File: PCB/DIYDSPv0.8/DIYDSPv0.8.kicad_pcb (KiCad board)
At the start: 4 copper layers, 100 x 80 mm, 199 parts, among them J1 Conn_01x06, J2 Conn_01x04, J3 Conn_01x04, J4 Conn_01x05, J5 Conn_01x01, J6 Conn_01x02, U1 ADAU1452, U5 AMS1117-1.2, X1 12.288MHz

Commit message: Updating progress on v0.8 design
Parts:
- removed C1, C14, C19, C24, C25, C27, C3, C31, C32, C34, C51: 10u, Capacitor_SMD:C_0603_1608Metric
- removed C10, C11, C12, C55, C7: 22u, Capacitor_SMD:C_0805_2012Metric
- removed C13, C17, C18, C20, C21, C26, C28, C29, C30, C33, C39, C43, C44, C45, C46, C48, C5, C52, C53, C54, C56, C57, C6: 100n, Capacitor_SMD:C_0402_1005Metric
- removed C15, C16, C2, C4: 2.2u, Capacitor_SMD:C_0402_1005Metric
- removed C22, C23, C40, C41: 10n, Capacitor_SMD:C_0402_1005Metric
- removed C35: 4.7n, Capacitor_SMD:C_0402_1005Metric
- removed C36, C37, C49, C50, C58, C59, C60, C61, C62, C63, C64, C65, C66, C67, C68, C69, C70, C71, C72, C73, C74, C75, C76, C77, C78, C79, C80, C81: 1u, Capacitor_SMD:C_0402_1005Metric
- removed C38: 1n, Capacitor_SMD:C_0402_1005Metric
- removed C42: 100p, Capacitor_SMD:C_0402_1005Metric
- removed C47: 47p, Capacitor_SMD:C_0402_1005Metric
- removed C8, C9: 22p, Capacitor_SMD:C_0402_1005Metric
- removed CN1: ~, Custom:MX126-5.0-02P-GN01-Cu-S-A
- removed D1: ~, Custom:SMF20CA
- removed D2, D3, D4: LED, LED_SMD:LED_0805_2012Metric
- removed J1: Conn_01x06, Connector_PinHeader_2.54mm:PinHeader_1x06_P2.54mm_Vertical
- removed J2, J3: Conn_01x04, Connector_PinHeader_2.54mm:PinHeader_1x04_P2.54mm_Vertical
- removed J4: Conn_01x05, Connector_PinHeader_2.54mm:PinHeader_1x05_P2.54mm_Vertical
- removed J5: Conn_01x01, Connector_PinHeader_2.54mm:PinHeader_1x01_P2.54mm_Vertical
- removed J6: Conn_01x02, Connector_PinHeader_2.54mm:PinHeader_1x02_P2.54mm_Vertical
- removed R1, R10, R11, R17, R18, R19, R2, R23, R24, R3, R4, R5, R6, R7, R8, R9: 100, Resistor_SMD:R_0805_2012Metric
- removed R12, R13, R25, R26, R27, R28: 10k, Resistor_SMD:R_0402_1005Metric
- removed R14, R29, R30, R37, R38, R39, R40, R41, R42, R43, R44, R45, R46, R49, R50, R57, R58, R59, R60, R61, R62, R63, R64, R65, R66: 100k, Resistor_SMD:R_0402_1005Metric
- removed R15, R16: 2.2k, Resistor_SMD:R_0402_1005Metric
- removed R20: 1k, Resistor_SMD:R_0402_1005Metric
- removed R21, R22: 5.1k, Resistor_SMD:R_0402_1005Metric
- removed R31, R32, R33, R34, R35, R36, R47, R48, R51, R52, R53, R54, R55, R56, R67, R68: 220k, Resistor_SMD:R_0603_1608Metric
- removed TP1, TP3, TP4, TP6: TestPoint, TestPoint:TestPoint_THTPad_D4.0mm_Drill2.0mm
- removed TP10, TP11, TP12, TP13, TP14, TP15, TP2, TP5, TP7, TP8, TP9: TestPoint, TestPoint:TestPoint_THTPad_D2.0mm_Drill1.0mm
- removed U1: ADAU1452, Custom:ADAU1452WBCPZ-RL
- removed U10: ~, Custom:GT-USB-7010ASV
- removed U11, U12, U13, U14, U15, U16, U8, U9: ~, Custom:PJ-320D
- removed U17: ~, Custom:ESP32-S3-WROOM-1U-N8
- removed U18, U19, U7: ~, Custom:YTS1C0033BBG01
- removed U2, U3: ~, Custom:AK4619VN
- removed U20, U21, U22, U23: ~, Custom:LM324DT
- removed U4: ~, Custom:K7803M-1000R3
- removed U5: AMS1117-1.2, Custom:AMS1117-1.2
- removed U6: ~, Custom:ADM811TARTZ-REEL7
- removed X1: 12.288MHz, Custom:S47SMD12.288M20PF20R30B3
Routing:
- net +1V2: track 117.7 -> 0.00 mm, vias 4 -> 0
- net GND: track 99.5 -> 0.00 mm, vias 102 -> 0
- net /SCL: track 89.6 -> 0.00 mm, vias 5 -> 0
- net /SDA: track 89.5 -> 0.00 mm, vias 5 -> 0
- net +3V3: track 80.3 -> 0.00 mm, vias 17 -> 0
- net /DAC_OUT8: track 78.8 -> 0.00 mm, vias 2 -> 0
- net /DAC_OUT7: track 72.9 -> 0.00 mm, vias 2 -> 0
- net /DAC_OUT4: track 72.9 -> 0.00 mm, vias 2 -> 0
- net /MCLK: track 72.8 -> 0.00 mm, vias 3 -> 0
- net /DAC_OUT3: track 68.1 -> 0.00 mm, vias 2 -> 0
- net /DAC_OUT6: track 66.1 -> 0.00 mm, vias 2 -> 0
- net /DAC_OUT5: track 65.9 -> 0.00 mm, vias 2 -> 0
- net /DAC_OUT1: track 64.6 -> 0.00 mm, vias 2 -> 0
- net /DAC_OUT2: track 63.0 -> 0.00 mm, vias 2 -> 0
- net /LRCLK_OUT0: track 59.5 -> 0.00 mm, vias 2 -> 0
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- removed copper zone on In2.Cu, net +12V
- removed copper zone on In2.Cu, net +3V3
- removed copper zone on B.Cu, net GND
- removed copper zone on F.Cu, net GND
- removed copper zone on In1.Cu, net GND
- removed copper zone on In2.Cu, net GND
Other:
- board outline removed
- board text removed: "+ -"
- board text removed: "1/2"
- board text removed: "12V"
- board text removed: "12V DC"
- board text removed: "1V2"
- board text removed: "3/4"
- board text removed: "3V3"
- board text removed: "5/6"
- board text removed: "7/8"
- board text removed: "ANALOG INPUT"
- board text removed: "ANALOG OUTPUT"
- board text removed: "AUXADC 0-5"
- board text removed: "BOOT"
- board text removed: "GND-3V3"
- board text removed: "GND-TX-RX"
- board text removed: "MCL-DSP8x8 V0.7"
- board text removed: "MP 0-3,6"
- board text removed: "Michael Larson"
- board text removed: "Optional BOOT Pull-Up"
- board text removed: "RESET"
- board text removed: "SCL SDA"

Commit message: More progress on V0.8 layout. Still trying to figure out analog placement.
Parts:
- added C1: 10u, Capacitor_SMD:C_0603_1608Metric, F.Cu at (113.9, 75.3)
- added C10: 2.2u, Capacitor_SMD:C_0402_1005Metric, F.Cu at (92.1, 84.6)
- added C100: 220uF, Custom:RVT1V221M0810, F.Cu at (65.1, 30.4)
- added C101: 10u, Capacitor_SMD:C_0603_1608Metric, F.Cu at (214.8, 91.0)
- added C102: 10u, Capacitor_SMD:C_0603_1608Metric, F.Cu at (214.8, 93.5)
- added C103: 22u, Capacitor_SMD:C_0805_2012Metric, F.Cu at (59.0, 35.1)
- added C104: 22u, Capacitor_SMD:C_0805_2012Metric, F.Cu at (82.5, 42.3)
- added C105: 100n, Capacitor_SMD:C_0402_1005Metric, F.Cu at (181.7, 81.1)
- added C106: 100n, Capacitor_SMD:C_0402_1005Metric, F.Cu at (181.7, 83.1)
- added C107: 220uF, Custom:RVT1V221M0810, F.Cu at (46.7, 30.4)
- added C108: 10u, Capacitor_SMD:C_0603_1608Metric, F.Cu at (214.8, 96.0)
- added C109: 10u, Capacitor_SMD:C_0603_1608Metric, F.Cu at (214.8, 98.5)
- added C11: 100n, Capacitor_SMD:C_0402_1005Metric, F.Cu at (111.2, 84.3)
- added C110: 22u, Capacitor_SMD:C_0805_2012Metric, F.Cu at (53.0, 33.8)
- added C111: 22u, Capacitor_SMD:C_0805_2012Metric, F.Cu at (50.5, 37.2)
- added C112: 10u, Capacitor_SMD:C_0603_1608Metric, F.Cu at (214.8, 101.0)
- added C113: 10u, Capacitor_SMD:C_0603_1608Metric, F.Cu at (214.8, 103.5)
- added C114: 100n, Capacitor_SMD:C_0402_1005Metric, F.Cu at (181.7, 85.1)
- added C115: 100n, Capacitor_SMD:C_0402_1005Metric, F.Cu at (181.7, 87.0)
- added C116: 100n, Capacitor_SMD:C_0402_1005Metric, F.Cu at (37.2, 43.7)
- added C12: 100n, Capacitor_SMD:C_0402_1005Metric, F.Cu at (93.4, 84.6)
- added C13: 10u, Capacitor_SMD:C_0603_1608Metric, F.Cu at (115.9, 84.8)
- added C14: 100n, Capacitor_SMD:C_0402_1005Metric, F.Cu at (106.0, 59.6)
- added C15: 100n, Capacitor_SMD:C_0402_1005Metric, F.Cu at (105.5, 66.0)
- added C16: 10n, Capacitor_SMD:C_0402_1005Metric, F.Cu at (103.2, 67.7)
- added C17: 10n, Capacitor_SMD:C_0402_1005Metric, F.Cu at (94.6, 55.4)
- added C18: 10u, Capacitor_SMD:C_0603_1608Metric, F.Cu at (98.2, 85.1)
- added C19: 100n, Capacitor_SMD:C_0402_1005Metric, F.Cu at (82.6, 45.6)
- added C2: 2.2u, Capacitor_SMD:C_0402_1005Metric, F.Cu at (111.7, 75.7)
- added C20: 10u, Capacitor_SMD:C_0603_1608Metric, F.Cu at (108.6, 84.8)
- added C21: 10u, Capacitor_SMD:C_0603_1608Metric, F.Cu at (90.8, 85.1)
- added C22: 100n, Capacitor_SMD:C_0402_1005Metric, F.Cu at (103.2, 68.7)
- added C23: 100n, Capacitor_SMD:C_0402_1005Metric, F.Cu at (94.6, 54.4)
- added C24: 100n, Capacitor_SMD:C_0402_1005Metric, F.Cu at (112.2, 84.3)
- added C25: 10u, Capacitor_SMD:C_0603_1608Metric, F.Cu at (109.6, 58.7)
- added C26: 10u, Capacitor_SMD:C_0603_1608Metric, F.Cu at (108.7, 64.1)
- added C27: 100n, Capacitor_SMD:C_0402_1005Metric, F.Cu at (94.4, 84.6)
- added C28: 10u, Capacitor_SMD:C_0603_1608Metric, F.Cu at (80.7, 47.5)
- added C29: 4.7n, Capacitor_SMD:C_0402_1005Metric, F.Cu at (107.8, 58.7)
- added C3: 10u, Capacitor_SMD:C_0603_1608Metric, F.Cu at (96.3, 75.5)
- added C30: 1u, Capacitor_SMD:C_0402_1005Metric, F.Cu at (103.2, 69.7)
- added C31: 1u, Capacitor_SMD:C_0402_1005Metric, F.Cu at (94.6, 53.4)
- added C32: 1n, Capacitor_SMD:C_0402_1005Metric, F.Cu at (107.8, 57.7)
- added C33: 100n, Capacitor_SMD:C_0402_1005Metric, F.Cu at (105.5, 56.3)
- added C34: 10n, Capacitor_SMD:C_0402_1005Metric, F.Cu at (103.3, 55.4)
- added C35: 10n, Capacitor_SMD:C_0402_1005Metric, F.Cu at (92.6, 66.0)
- added C36: 100n, Capacitor_SMD:C_0402_1005Metric, F.Cu at (105.4, 63.8)
- added C37: 100p, Capacitor_SMD:C_0402_1005Metric, F.Cu at (105.5, 58.2)
- added C38: 100n, Capacitor_SMD:C_0402_1005Metric, F.Cu at (170.2, 79.2)
- added C39: 100n, Capacitor_SMD:C_0402_1005Metric, F.Cu at (92.5, 57.2)
- added C4: 2.2u, Capacitor_SMD:C_0402_1005Metric, F.Cu at (94.0, 76.0)
- added C40: 100n, Capacitor_SMD:C_0402_1005Metric, F.Cu at (103.3, 54.4)
- added C41: 100n, Capacitor_SMD:C_0402_1005Metric, F.Cu at (91.6, 66.0)
- added C42: 10u, Capacitor_SMD:C_0603_1608Metric, F.Cu at (108.0, 66.3)
- added C43: 47p, Capacitor_SMD:C_0402_1005Metric, F.Cu at (106.5, 58.2)
- added C44: 10u, Capacitor_SMD:C_0603_1608Metric, F.Cu at (206.8, 96.0)
- added C45: 1u, Capacitor_SMD:C_0402_1005Metric, F.Cu at (103.3, 53.4)
- added C46: 1u, Capacitor_SMD:C_0402_1005Metric, F.Cu at (90.6, 66.0)
- added C47: 100n, Capacitor_SMD:C_0402_1005Metric, F.Cu at (94.3, 67.8)
- added C48: 100n, Capacitor_SMD:C_0402_1005Metric, F.Cu at (94.7, 29.3)
- added C49: 100n, Capacitor_SMD:C_0402_1005Metric, F.Cu at (120.4, 44.7)
- added C5: 100n, Capacitor_SMD:C_0402_1005Metric, F.Cu at (112.7, 75.7)
- added C50: 22u, Capacitor_SMD:C_0805_2012Metric, F.Cu at (94.0, 26.0)
- added C51: 100n, Capacitor_SMD:C_0402_1005Metric, F.Cu at (91.9, 37.9)
- added C52: 100n, Capacitor_SMD:C_0402_1005Metric, F.Cu at (95.9, 28.0)
- added C53: 100n, Capacitor_SMD:C_0402_1005Metric, F.Cu at (95.9, 40.0)
- added C54: 1u, Capacitor_SMD:C_0402_1005Metric, F.Cu at (173.1, 85.1)
- added C55: 1u, Capacitor_SMD:C_0402_1005Metric, F.Cu at (173.1, 87.0)
- added C56: 1u, Capacitor_SMD:C_0402_1005Metric, F.Cu at (173.1, 89.0)
- added C57: 1u, Capacitor_SMD:C_0402_1005Metric, F.Cu at (175.9, 69.3)
- added C58: 10u, Capacitor_SMD:C_0603_1608Metric, F.Cu at (206.8, 101.0)
- added C59: 10u, Capacitor_SMD:C_0603_1608Metric, F.Cu at (206.8, 103.5)
- added C6: 100n, Capacitor_SMD:C_0402_1005Metric, F.Cu at (95.0, 76.0)
- added C60: 100n, Capacitor_SMD:C_0402_1005Metric, F.Cu at (40.2, 36.3)
- added C61: 22u, Capacitor_SMD:C_0805_2012Metric, F.Cu at (52.9, 29.0)
- added C62: 100n, Capacitor_SMD:C_0402_1005Metric, F.Cu at (175.9, 73.3)
- added C63: 100n, Capacitor_SMD:C_0402_1005Metric, F.Cu at (175.9, 75.2)
- added C64: 10u, Capacitor_SMD:C_0603_1608Metric, F.Cu at (206.8, 106.0)
- added C65: 10u, Capacitor_SMD:C_0603_1608Metric, F.Cu at (210.8, 91.0)
- added C66: 100n, Capacitor_SMD:C_0402_1005Metric, F.Cu at (175.9, 77.2)
- added C67: 100n, Capacitor_SMD:C_0402_1005Metric, F.Cu at (175.9, 79.2)
- added C68: 220uF, Custom:RVT1V221M0810, F.Cu at (37.8, 30.4)
- added C69: 1u, Capacitor_SMD:C_0402_1005Metric, F.Cu at (175.9, 81.1)
- added C7: 22p, Capacitor_SMD:C_0402_1005Metric, F.Cu at (109.3, 56.3)
- added C70: 1u, Capacitor_SMD:C_0402_1005Metric, F.Cu at (175.9, 83.1)
- added C71: 1u, Capacitor_SMD:C_0402_1005Metric, F.Cu at (175.9, 85.1)
- added C72: 1u, Capacitor_SMD:C_0402_1005Metric, F.Cu at (175.9, 87.0)
- added C73: 100n, Capacitor_SMD:C_0402_1005Metric, F.Cu at (175.9, 89.0)
- added C74: 100n, Capacitor_SMD:C_0402_1005Metric, F.Cu at (178.8, 69.3)
- added C75: 100n, Capacitor_SMD:C_0402_1005Metric, F.Cu at (72.3, 27.3)
- added C76: 10u, Capacitor_SMD:C_0603_1608Metric, F.Cu at (210.8, 93.5)
- added C77: 10u, Capacitor_SMD:C_0603_1608Metric, F.Cu at (210.8, 96.0)
- added C78: 22u, Capacitor_SMD:C_0805_2012Metric, F.Cu at (83.8, 34.8)
- added C79: 1u, Capacitor_SMD:C_0402_1005Metric, F.Cu at (178.8, 73.3)
- added C8: 22p, Capacitor_SMD:C_0402_1005Metric, F.Cu at (112.3, 50.2)
- added C80: 1u, Capacitor_SMD:C_0402_1005Metric, F.Cu at (178.8, 75.2)
- added C81: 1u, Capacitor_SMD:C_0402_1005Metric, F.Cu at (178.8, 77.2)
- added C82: 1u, Capacitor_SMD:C_0402_1005Metric, F.Cu at (178.8, 79.2)
- added C83: 220uF, Custom:RVT1V221M0810, F.Cu at (77.7, 30.4)
- added C84: 10u, Capacitor_SMD:C_0603_1608Metric, F.Cu at (210.8, 98.5)
- added C85: 10u, Capacitor_SMD:C_0603_1608Metric, F.Cu at (210.8, 101.0)
- added C86: 100n, Capacitor_SMD:C_0402_1005Metric, F.Cu at (178.8, 81.1)
- added C87: 100n, Capacitor_SMD:C_0402_1005Metric, F.Cu at (178.8, 83.1)
- added C88: 100n, Capacitor_SMD:C_0402_1005Metric, F.Cu at (178.8, 85.1)
- added C89: 100n, Capacitor_SMD:C_0402_1005Metric, F.Cu at (178.8, 87.0)
- added C9: 2.2u, Capacitor_SMD:C_0402_1005Metric, F.Cu at (109.9, 84.3)
- added C90: 1u, Capacitor_SMD:C_0402_1005Metric, F.Cu at (178.8, 89.0)
- added C91: 1u, Capacitor_SMD:C_0402_1005Metric, F.Cu at (181.7, 69.3)
- added C92: 1u, Capacitor_SMD:C_0402_1005Metric, F.Cu at (18.7, 45.2)
- added C93: 1u, Capacitor_SMD:C_0402_1005Metric, F.Cu at (19.0, 48.6)
- added C94: 100n, Capacitor_SMD:C_0402_1005Metric, F.Cu at (58.5, 32.3)
- added C95: 22u, Capacitor_SMD:C_0805_2012Metric, F.Cu at (59.0, 29.5)
- added C96: 10u, Capacitor_SMD:C_0603_1608Metric, F.Cu at (210.8, 103.5)
- added C97: 10u, Capacitor_SMD:C_0603_1608Metric, F.Cu at (210.8, 106.0)
- added C98: 100n, Capacitor_SMD:C_0402_1005Metric, F.Cu at (181.7, 77.2)
- added C99: 100n, Capacitor_SMD:C_0402_1005Metric, F.Cu at (181.7, 79.2)
- added CN1: ~, Custom:MX126-5.0-02P-GN01-Cu-S-A, F.Cu at (29.1, 37.8)
- added D1: LED, LED_SMD:LED_0805_2012Metric, F.Cu at (160.8, 93.9)
- added D2: LED, LED_SMD:LED_0805_2012Metric, F.Cu at (117.0, 27.2)
- added D3: ~, Custom:CUS08F30,H3F, F.Cu at (34.3, 37.6)
- added D4: ~, Custom:CUS08F30,H3F, F.Cu at (71.4, 25.9)
- added D5: ~, Custom:CUS08F30,H3F, F.Cu at (53.9, 26.0)
- added D6: ~, Custom:SMF20CA, F.Cu at (58.2, 26.1)
- added D7: LED, LED_SMD:LED_0805_2012Metric, F.Cu at (73.4, 51.0)
- added D8: LED, LED_SMD:LED_0805_2012Metric, F.Cu at (49.4, 41.3)
- added H1: MountingHole_Pad, MountingHole:MountingHole_3.2mm_M3_Pad_TopBottom, F.Cu at (28.5, 28.5)
- added H2: MountingHole_Pad, MountingHole:MountingHole_3.2mm_M3_Pad_TopBottom, F.Cu at (121.5, 28.5)
- added H3: MountingHole_Pad, MountingHole:MountingHole_3.2mm_M3_Pad_TopBottom, F.Cu at (28.5, 86.5)
- added H4: MountingHole_Pad, MountingHole:MountingHole_3.2mm_M3_Pad_TopBottom, F.Cu at (121.5, 86.5)
- added J1: Conn_01x06, Connector_PinHeader_2.54mm:PinHeader_1x06_P2.54mm_Vertical, F.Cu at (122.7, 71.1)
- added J10: Conn_01x05, Connector_PinHeader_2.54mm:PinHeader_1x05_P2.54mm_Vertical, F.Cu at (30.6, 55.4)
- added J11: Conn_01x05, Connector_PinHeader_2.54mm:PinHeader_1x05_P2.54mm_Vertical, F.Cu at (112.5, 152.7)
- added J12: Conn_01x05, Connector_PinHeader_2.54mm:PinHeader_1x05_P2.54mm_Vertical, F.Cu at (26.8, 55.1)
- added J13: Conn_01x05, Connector_PinHeader_2.54mm:PinHeader_1x05_P2.54mm_Vertical, F.Cu at (49.5, 74.4)
- added J2: Conn_01x05, Connector_PinHeader_2.54mm:PinHeader_1x05_P2.54mm_Vertical, F.Cu at (101.4, 50.5)
- added J3: Conn_01x04, Connector_PinHeader_2.54mm:PinHeader_1x04_P2.54mm_Vertical, F.Cu at (118.3, 33.8)
- added J4: Conn_01x04, Connector_PinHeader_2.54mm:PinHeader_1x04_P2.54mm_Vertical, F.Cu at (67.0, 40.6)
- added J5: Conn_01x02, Connector_PinHeader_2.54mm:PinHeader_1x02_P2.54mm_Vertical, F.Cu at (101.7, 100.4)
- added J6: Conn_01x05, Connector_PinHeader_2.54mm:PinHeader_1x05_P2.54mm_Vertical, F.Cu at (32.3, 150.0)
- added J7: Conn_01x05, Connector_PinHeader_2.54mm:PinHeader_1x05_P2.54mm_Vertical, F.Cu at (112.5, 145.5)
- added J8: Conn_01x05, Connector_PinHeader_2.54mm:PinHeader_1x05_P2.54mm_Vertical, F.Cu at (27.2, 70.9)
- added J9: Conn_01x05, Connector_PinHeader_2.54mm:PinHeader_1x05_P2.54mm_Vertical, F.Cu at (112.5, 149.1)
- added R1: 100, Resistor_SMD:R_0805_2012Metric, F.Cu at (109.6, 49.7)
- added R10: 100, Resistor_SMD:R_0805_2012Metric, F.Cu at (116.9, 77.8)
- added R11: 100, Resistor_SMD:R_0805_2012Metric, F.Cu at (99.2, 78.0)
- added R12: 10k, Resistor_SMD:R_0402_1005Metric, F.Cu at (117.5, 80.8)
- added R13: 10k, Resistor_SMD:R_0402_1005Metric, F.Cu at (99.8, 81.0)
- added R14: 100, Resistor_SMD:R_0805_2012Metric, F.Cu at (194.1, 100.1)
- added R15: 1k, Resistor_SMD:R_0402_1005Metric, F.Cu at (179.8, 54.4)
- added R16: 2.2k, Resistor_SMD:R_0402_1005Metric, F.Cu at (108.3, 56.3)
- added R17: 2.2k, Resistor_SMD:R_0402_1005Metric, F.Cu at (107.3, 56.3)
- added R18: 1k, Resistor_SMD:R_0402_1005Metric, F.Cu at (100.6, 46.3)
- added R19: 100, Resistor_SMD:R_0805_2012Metric, F.Cu at (88.7, 36.6)
- added R2: 100, Resistor_SMD:R_0805_2012Metric, F.Cu at (110.2, 74.7)
- added R20: 100, Resistor_SMD:R_0805_2012Metric, F.Cu at (86.8, 36.6)
- added R21: 10k, Resistor_SMD:R_0402_1005Metric, F.Cu at (93.4, 33.4)
- added R22: 100k, Resistor_SMD:R_0402_1005Metric, F.Cu at (91.6, 35.0)
- added R23: 5.1k, Resistor_SMD:R_0402_1005Metric, F.Cu at (93.1, 29.3)
- added R24: 5.1k, Resistor_SMD:R_0402_1005Metric, F.Cu at (84.5, 37.6)
- added R25: 100, Resistor_SMD:R_0805_2012Metric, F.Cu at (122.1, 34.3)
- added R26: 10k, Resistor_SMD:R_0402_1005Metric, F.Cu at (107.7, 100.0)
- added R27: 10k, Resistor_SMD:R_0402_1005Metric, F.Cu at (107.7, 102.0)
- added R28: 1k, Resistor_SMD:R_0402_1005Metric, F.Cu at (182.8, 46.6)
- added R29: 1k, Resistor_SMD:R_0402_1005Metric, F.Cu at (182.8, 48.6)
- added R3: 100, Resistor_SMD:R_0805_2012Metric, F.Cu at (108.3, 74.7)
- added R30: 100k, Resistor_SMD:R_0402_1005Metric, F.Cu at (182.8, 50.6)
- added R31: 100k, Resistor_SMD:R_0402_1005Metric, F.Cu at (182.8, 52.5)
- added R32: 100k, Resistor_SMD:R_0402_1005Metric, F.Cu at (182.8, 54.5)
- added R33: 100k, Resistor_SMD:R_0402_1005Metric, F.Cu at (182.8, 56.5)
- added R34: 100k, Resistor_SMD:R_0402_1005Metric, F.Cu at (182.8, 58.5)
- added R35: 100k, Resistor_SMD:R_0402_1005Metric, F.Cu at (185.8, 42.6)
- added R36: 100k, Resistor_SMD:R_0402_1005Metric, F.Cu at (185.8, 44.6)
- added R37: 100k, Resistor_SMD:R_0402_1005Metric, F.Cu at (185.8, 46.6)
- added R38: 100k, Resistor_SMD:R_0402_1005Metric, F.Cu at (185.8, 48.6)
- added R39: 100k, Resistor_SMD:R_0402_1005Metric, F.Cu at (185.8, 50.6)
- added R4: 100, Resistor_SMD:R_0805_2012Metric, F.Cu at (106.4, 74.7)
- added R40: 100k, Resistor_SMD:R_0402_1005Metric, F.Cu at (185.8, 52.5)
- added R41: 100k, Resistor_SMD:R_0402_1005Metric, F.Cu at (185.8, 54.5)
- added R42: 100k, Resistor_SMD:R_0402_1005Metric, F.Cu at (185.8, 56.5)
- added R43: 100k, Resistor_SMD:R_0402_1005Metric, F.Cu at (185.8, 58.5)
- added R44: 1k, Resistor_SMD:R_0402_1005Metric, F.Cu at (188.7, 42.6)
- added R45: 1k, Resistor_SMD:R_0402_1005Metric, F.Cu at (188.7, 44.6)
- added R46: 100k, Resistor_SMD:R_0402_1005Metric, F.Cu at (188.7, 46.6)
- added R47: 100k, Resistor_SMD:R_0402_1005Metric, F.Cu at (188.7, 48.6)
- added R48: 100k, Resistor_SMD:R_0402_1005Metric, F.Cu at (188.7, 50.6)
- added R49: 100k, Resistor_SMD:R_0402_1005Metric, F.Cu at (188.7, 52.5)
- added R5: 100, Resistor_SMD:R_0805_2012Metric, F.Cu at (92.5, 74.7)
- added R50: 100k, Resistor_SMD:R_0402_1005Metric, F.Cu at (188.7, 54.5)
- added R51: 100k, Resistor_SMD:R_0402_1005Metric, F.Cu at (188.7, 56.5)
- added R52: 100k, Resistor_SMD:R_0402_1005Metric, F.Cu at (188.7, 58.5)
- added R53: 100k, Resistor_SMD:R_0402_1005Metric, F.Cu at (191.6, 42.6)
- added R54: 100k, Resistor_SMD:R_0402_1005Metric, F.Cu at (191.6, 44.6)
- added R55: 100k, Resistor_SMD:R_0402_1005Metric, F.Cu at (191.6, 46.6)
- added R56: 1k, Resistor_SMD:R_0402_1005Metric, F.Cu at (191.6, 48.6)
- added R57: 1k, Resistor_SMD:R_0402_1005Metric, F.Cu at (191.6, 50.6)
- added R58: 100k, Resistor_SMD:R_0402_1005Metric, F.Cu at (191.6, 52.5)
- added R59: 100k, Resistor_SMD:R_0402_1005Metric, F.Cu at (191.6, 54.5)
- added R6: 100, Resistor_SMD:R_0805_2012Metric, F.Cu at (90.6, 74.7)
- added R60: 100k, Resistor_SMD:R_0402_1005Metric, F.Cu at (191.6, 56.5)
- added R61: 100k, Resistor_SMD:R_0402_1005Metric, F.Cu at (191.6, 58.5)
- added R62: 100k, Resistor_SMD:R_0402_1005Metric, F.Cu at (4.09, 41.7)
- added R63: 100k, Resistor_SMD:R_0402_1005Metric, F.Cu at (4.09, 42.7)
- added R64: 100k, Resistor_SMD:R_0402_1005Metric, F.Cu at (194.5, 46.6)
- added R65: 100k, Resistor_SMD:R_0402_1005Metric, F.Cu at (194.5, 48.6)
- added R66: 100k, Resistor_SMD:R_0402_1005Metric, F.Cu at (194.5, 50.6)
- added R67: 100k, Resistor_SMD:R_0402_1005Metric, F.Cu at (194.5, 52.5)
- added R68: 100k, Resistor_SMD:R_0402_1005Metric, F.Cu at (43.8, 38.2)
- added R69: 100k, Resistor_SMD:R_0402_1005Metric, F.Cu at (42.7, 38.2)
- added R7: 100, Resistor_SMD:R_0805_2012Metric, F.Cu at (88.7, 74.7)
- added R70: 1k, Resistor_SMD:R_0402_1005Metric, F.Cu at (194.5, 58.5)
- added R71: 1k, Resistor_SMD:R_0402_1005Metric, F.Cu at (197.4, 42.6)
- added R72: 100k, Resistor_SMD:R_0402_1005Metric, F.Cu at (197.4, 44.6)
- added R73: 100k, Resistor_SMD:R_0402_1005Metric, F.Cu at (197.4, 46.6)
- added R74: 100, Resistor_SMD:R_0805_2012Metric, F.Cu at (76.8, 51.0)
- added R75: 100k, Resistor_SMD:R_0402_1005Metric, F.Cu at (39.3, 38.2)
- added R76: 100k, Resistor_SMD:R_0402_1005Metric, F.Cu at (38.2, 38.2)
- added R77: 100k, Resistor_SMD:R_0402_1005Metric, F.Cu at (197.4, 52.5)
- added R78: 100k, Resistor_SMD:R_0402_1005Metric, F.Cu at (197.4, 54.5)
- added R79: 100k, Resistor_SMD:R_0402_1005Metric, F.Cu at (197.4, 56.5)
- added R8: 100, Resistor_SMD:R_0805_2012Metric, F.Cu at (115.6, 75.1)
- added R80: 100k, Resistor_SMD:R_0402_1005Metric, F.Cu at (197.4, 58.5)
- added R81: 100, Resistor_SMD:R_0805_2012Metric, F.Cu at (51.4, 41.3)
- added R9: 100, Resistor_SMD:R_0805_2012Metric, F.Cu at (98.0, 75.3)
- added SW1: ~, Custom:TS110916043, F.Cu at (117.2, 50.2)
- added SW2: ~, Custom:TS110916043, F.Cu at (122.4, 50.2)
- added SW3: ~, Custom:TS110916043, F.Cu at (91.4, 43.5)
- added TP1: TestPoint, TestPoint:TestPoint_THTPad_D4.0mm_Drill2.0mm, F.Cu at (186.1, 62.5)
- added TP2: TestPoint, TestPoint:TestPoint_THTPad_D2.0mm_Drill1.0mm, F.Cu at (200.9, 43.6)
- added TP3: TestPoint, TestPoint:TestPoint_THTPad_D2.0mm_Drill1.0mm, F.Cu at (34.9, 41.0)
- added TP4: TestPoint, TestPoint:TestPoint_THTPad_D2.0mm_Drill1.0mm, F.Cu at (71.4, 31.0)
- added TP5: TestPoint, TestPoint:TestPoint_THTPad_D2.0mm_Drill1.0mm, F.Cu at (71.4, 35.1)
- added TP6: TestPoint, TestPoint:TestPoint_THTPad_D2.0mm_Drill1.0mm, F.Cu at (80.9, 37.4)
- added TP7: TestPoint, TestPoint:TestPoint_THTPad_D2.0mm_Drill1.0mm, F.Cu at (47.0, 38.6)
- added U1: ADAU1452, Custom:ADAU1452WBCPZ-RL, F.Cu at (98.9, 61.6)
- added U10: ~, Custom:TLV9062IDR, F.Cu at (5.99, 80.0)
- added U11: ~, Custom:TLV9062IDR, F.Cu at (5.97, 58.4)
- added U12: ~, Custom:TLV9062IDR, F.Cu at (0.38, 74.6)
- added U13: ~, Custom:TLV9062IDR, F.Cu at (0.38, 53.0)
- added U14: ~, Custom:TLV9062IDR, F.Cu at (144.6, 130.2)
- added U15: ~, Custom:TLV9062IDR, F.Cu at (151.2, 130.2)
- added U16: ~, Custom:TLV9062IDR, F.Cu at (5.97, 69.2)
- added U17: ~, Custom:TLV9062IDR, F.Cu at (5.99, 47.6)
- added U18: ~, Custom:TLV9062IDR, F.Cu at (171.0, 130.2)
- added U19: ~, Custom:TLV9062IDR, F.Cu at (177.6, 130.2)
- added U2: ~, Custom:AK4619VN, F.Cu at (111.9, 80.0)
- added U20: ~, Custom:TLV9062IDR, F.Cu at (0.38, 63.8)
- added U21: ~, Custom:TLV9062IDR, F.Cu at (0.38, 42.2)
- added U22: ~, Custom:TLV9062IDR, F.Cu at (41.7, 42.3)
- added U23: ~, Custom:K7803-1000, F.Cu at (77.0, 43.9)
- added U24: ~, Custom:TLV9062IDR, F.Cu at (164.4, 139.1)
- added U25: ~, Custom:TLV9062IDR, F.Cu at (57.8, 56.9)
- added U26: ~, Custom:K7803-1000, F.Cu at (58.6, 45.1)
- added U3: ~, Custom:AK4619VN, F.Cu at (94.2, 80.3)
- added U4: AMS1117-1.2, Custom:AMS1117-1.2, F.Cu at (85.0, 50.5)
- added U5: ~, Custom:ESP32-S3-WROOM-1U-N8, F.Cu at (106.2, 35.9)
- added U6: ~, Custom:ADM811TARTZ-REEL7, F.Cu at (94.2, 37.2)
- added U7: ~, Custom:GT-USB-7010ASV, F.Cu at (87.3, 30.2)
- added U8: ~, Custom:TLV9062IDR, F.Cu at (144.6, 121.3)
- added U9: ~, Custom:TLV9062IDR, F.Cu at (151.2, 121.3)
- added X1: 12.288MHz, Custom:S47SMD12.288M20PF20R30B3, F.Cu at (109.1, 53.0)
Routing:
- net +3V3: track 0.00 -> 56.0 mm, vias 0 -> 1
- net VCC: track 0.00 -> 44.8 mm
- net /EN: track 0.00 -> 36.4 mm, vias 0 -> 2
- net +12V: track 0.00 -> 35.1 mm
- net VBUS: track 0.00 -> 32.2 mm, vias 0 -> 2
- net +3.3VA: track 0.00 -> 28.6 mm, vias 0 -> 6
- net /AUXADC0: track 0.00 -> 22.5 mm
- net /AUXADC1: track 0.00 -> 21.7 mm
- net /AUXADC2: track 0.00 -> 20.8 mm
- net /AUXADC3: track 0.00 -> 20.0 mm
- net /AUXADC5: track 0.00 -> 19.4 mm, vias 0 -> 1
- net /AUXADC4: track 0.00 -> 19.1 mm
- net /DSP_SS: track 0.00 -> 17.3 mm, vias 0 -> 2
- net /DSP_MOSI: track 0.00 -> 16.8 mm, vias 0 -> 2
- net /DSP_MISO: track 0.00 -> 16.6 mm, vias 0 -> 2
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- added copper zone on In2.Cu, net +3.3VA
- added copper zone on In2.Cu, net +3V3
- added copper zone on B.Cu, net GND
- added copper zone on F.Cu, net GND
- added copper zone on In1.Cu, net GND
- added copper zone on In2.Cu, net GND
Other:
- board outline added: 100 x 65 mm
- board text added: "Reset|Boot"

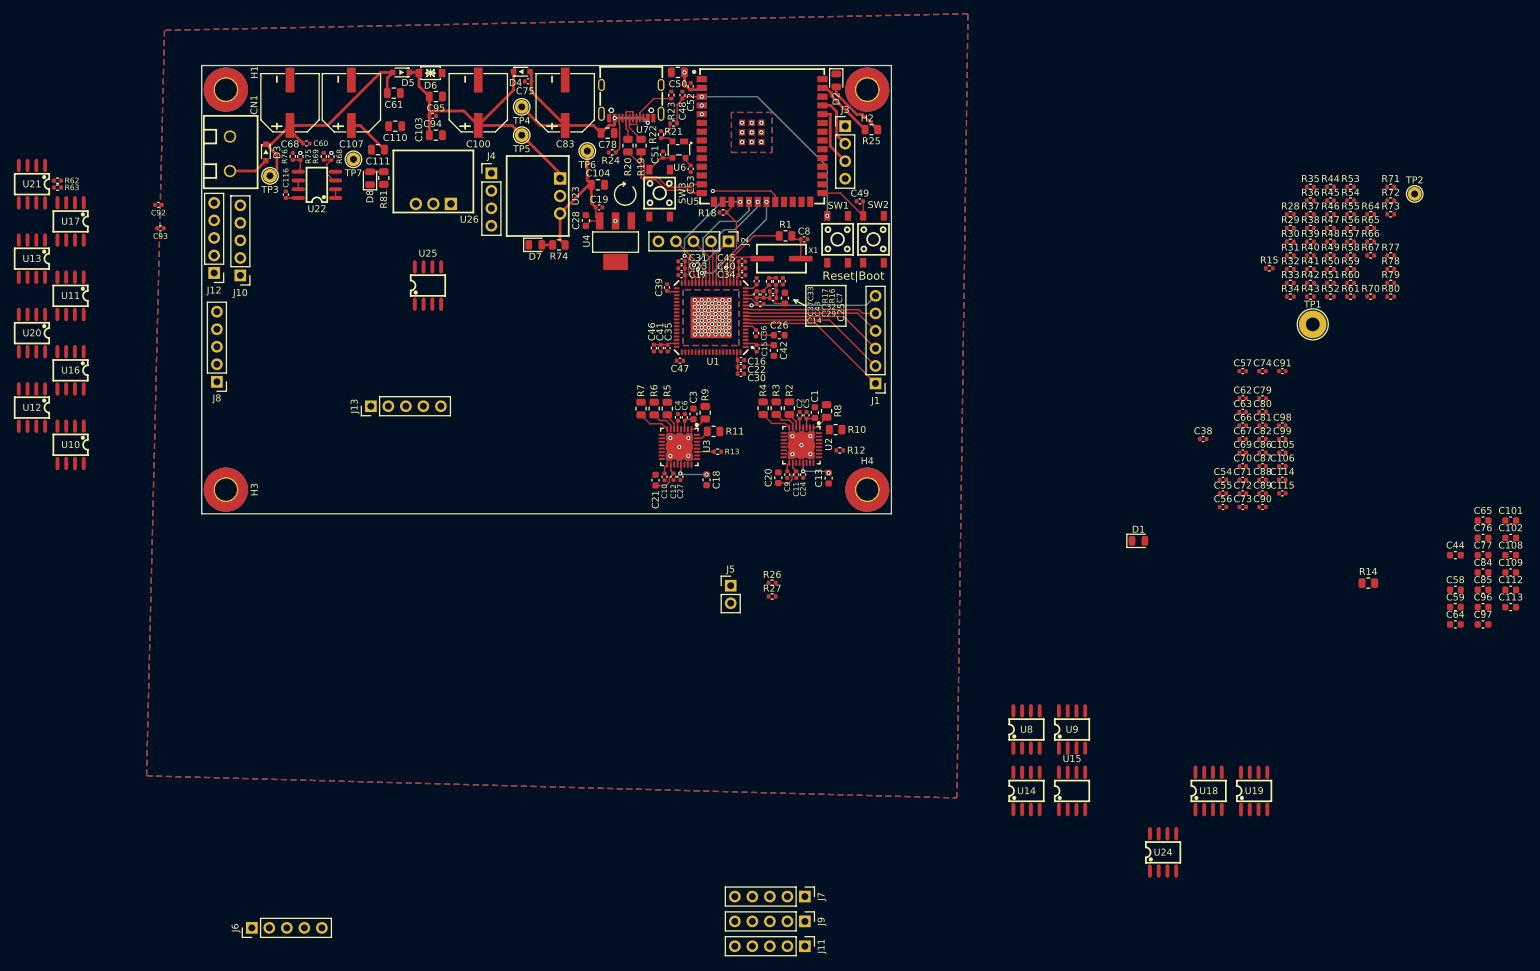
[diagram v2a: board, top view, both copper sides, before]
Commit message: Nearly done with v0.8 placement - Dealing with DRC errors
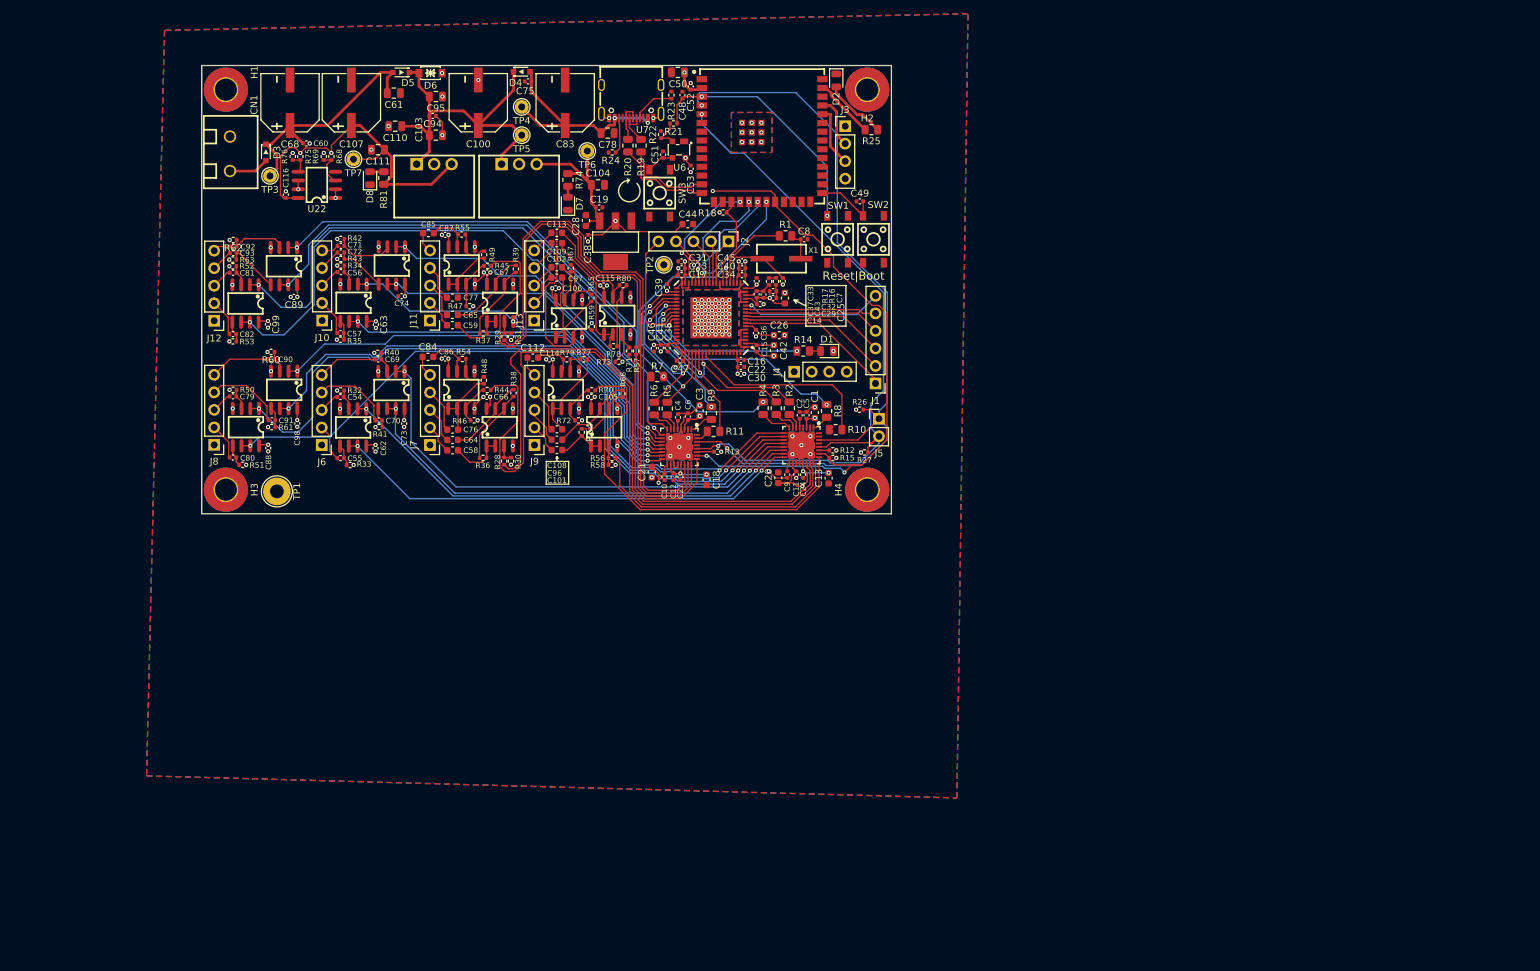
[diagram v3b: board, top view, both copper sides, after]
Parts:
- moved R53 163.6 mm to (29.5, 65.0)
- moved C85 161.4 mm to (57.9, 49.3)
- moved R50 160.1 mm to (29.5, 72.0), turned to 180 degrees
- moved R51 159.9 mm to (30.9, 82.9), turned to 180 degrees
- moved R52 159.2 mm to (29.5, 54.1), turned to 180 degrees
- moved R61 157.6 mm to (35.1, 77.4)
- moved R60 156.9 mm to (35.0, 66.5), turned to 180 degrees
- moved C84 156.1 mm to (57.8, 67.2)
- moved C77 154.0 mm to (61.4, 58.6)
- moved C65 152.4 mm to (61.4, 61.1)
- moved TP1 152.1 mm to (35.9, 86.8), turned to -90 degrees
- moved C59 151.1 mm to (61.4, 62.6)
- moved C81 150.9 mm to (29.6, 55.0), turned to 180 degrees
- moved C76 150.2 mm to (61.4, 77.8)
- moved C82 150.1 mm to (29.5, 64.0), turned to 180 degrees
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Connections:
- J11 pad 2: /AOUT_5N -> /AOUT_5P
- J11 pad 3: /AOUT_5P -> /AOUT_5N
- J11 pad 4: /AOUT_6N -> /AOUT_6P
- J11 pad 5: /AOUT_6P -> /AOUT_6N
- J13 pad 2: /AOUT_7N -> /AOUT_7P
- J13 pad 3: /AOUT_7P -> /AOUT_7N
- J13 pad 4: /AOUT_8N -> /AOUT_8P
- J13 pad 5: /AOUT_8P -> /AOUT_8N
- J7 pad 2: /AOUT_1N -> /AOUT_1P
- J7 pad 3: /AOUT_1P -> /AOUT_1N
- J7 pad 4: /AOUT_2N -> /AOUT_2P
- J7 pad 5: /AOUT_2P -> /AOUT_2N
- J9 pad 2: /AOUT_3N -> /AOUT_3P
- J9 pad 3: /AOUT_3P -> /AOUT_3N
- J9 pad 4: /AOUT_4N -> /AOUT_4P
- J9 pad 5: /AOUT_4P -> /AOUT_4N
- R10 pad 1: /SDATA_IN0 -> /SDATA_IN1
- R11 pad 1: /SDATA_IN1 -> /SDATA_IN0
- R2 pad 1: /LRCLK_OUT0 -> /LRCLK_OUT1
- R3 pad 1: /BCLK_OUT0 -> /BCLK_OUT1
- R5 pad 1: /LRCLK_OUT1 -> /LRCLK_OUT0
- R6 pad 1: /BCLK_OUT1 -> /BCLK_OUT0
- R8 pad 1: /SDATA_OUT0 -> /SDATA_OUT1
- R9 pad 1: /SDATA_OUT1 -> /SDATA_OUT0
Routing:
- net /1V65_2: track 1.27 -> 149.4 mm, vias 0 -> 17
- net /SDA: track 0.00 -> 116.3 mm, vias 1 -> 2
- net /1V65_1: track 1.27 -> 109.5 mm, vias 0 -> 17
- net /ADC_IN3N: track 0.00 -> 103.5 mm, vias 0 -> 2
- net /SCL: track 0.00 -> 102.3 mm, vias 1 -> 2
- net /DAC_OUT2: track 0.00 -> 102.1 mm
- net /ADC_IN3P: track 0.00 -> 99.9 mm, vias 0 -> 2
- net /DAC_OUT6: track 0.00 -> 98.8 mm
- net /ADC_IN4P: track 0.00 -> 94.3 mm, vias 0 -> 2
- net /ADC_IN7P: track 0.00 -> 92.6 mm, vias 0 -> 2
- net /ADC_IN7N: track 0.00 -> 90.6 mm, vias 0 -> 2
- net /ADC_IN4N: track 0.00 -> 88.8 mm, vias 0 -> 2
- net /DAC_OUT1: track 0.00 -> 85.0 mm
- net /ADC_IN8P: track 0.00 -> 81.1 mm, vias 0 -> 2
- net /DAC_OUT5: track 0.00 -> 80.2 mm
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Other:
- board text added: "1/2 IN"
- board text added: "1/2 OUT"
- board text added: "3/4 IN"
- board text added: "3/4 OUT"

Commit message: V0.8 Complete. Will be working on audio connector boards.
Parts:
- U23, U26: footprint Custom:K7803-1000 -> Custom:K7803-1000_C50396471
- moved U26 3.80 mm to (58.8, 43.1)
- moved U23 3.80 mm to (71.0, 43.1)
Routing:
- net /CODEC_EN: track 90.3 -> 80.0 mm, vias 3 -> 2
- net VCC: track 51.1 -> 58.7 mm
- net +3V3: track 62.0 -> 58.3 mm
- net GND: track 62.3 -> 65.0 mm
- net Net-(U2-SDOUT1): track 0.00 -> 2.38 mm
- net +3.3VA: track 102.7 -> 103.8 mm
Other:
- outline, holes or cut-outs redrawn
- board text added: "2- 2+ 1- 1+ GND"
- board text added: "4- 4+ 3- 3+ GND"
- board text added: "5 4 3 2 1 0"
- board text added: "6- 6+ 5- 5+ GND"
- board text added: "8- 8+ 7- 7+ GND"
- board text added: "ANALOG IN"
- board text added: "ANALOG OUT"
- board text added: "AUX ADC"
- board text added: "GND 3V3"
- board text added: "GND GND 3V3 3V3"
- board text added: "GND TX RX NC"
- board text added: "MCL-DSP8x8"
- board text added: "MP6 MP3 MP2 MP1 MP0"
- board text added: "Michael Larson"
- board text added: "SDA SCL"
- board text added: "V0.8"
- board text removed: "1/2 IN"
- board text removed: "1/2 OUT"
- board text removed: "3/4 IN"
- board text removed: "3/4 OUT"

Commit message: Fix analog connector labels on v0.8 main board.
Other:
- board text removed: "Michael Larson"
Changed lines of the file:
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@@
 		(at 94.25 80.3 -90)
 		(property "Reference" "U3"
-			(at 0 0 -90)
+			(at 0 0 270)
 			(layer "B.SilkS")
 			(effects
@@
 		(at 71.013858 43.1)
 		(property "Reference" "U23"
-			(at -0.013858 -1.65 -0)
+			(at -0.013858 -1.65 0)
 			(layer "B.SilkS")
 			(effects
@@
 		(at 106.25 35.875)
 		(property "Reference" "U5"
-			(at -0.195 -0.28125 -0)
+			(at -0.195 -0.28125 0)
 			(layer "B.SilkS")
 			(effects
@@
 		(at 58.8 43.1)
 		(property "Reference" "U26"
-			(at -0.013858 -1.65 -0)
+			(at -0.013858 -1.65 0)
 			(layer "B.SilkS")
 			(effects
@@
 		(at 85 50.505 90)
 		(property "Reference" "U4"
-			(at 0 0 -180)
+			(at 0 0 180)
 			(layer "B.SilkS")
 			(effects
@@
 		(at 111.9495 80.049 -90)
 		(property "Reference" "U2"
-			(at 0 0 -90)
+			(at 0 0 270)
 			(layer "B.SilkS")
 			(effects
@@
 		(at 98.86 61.5505 180)
 		(property "Reference" "U1"
-			(at -0.274 0 -0)
+			(at -0.274 0 0)
 			(layer "B.SilkS")
 			(effects
@@
 	)
 	(gr_text "2-\n\n2+\n\n1-\n\n1+\n\nGND"
-		(at 28.15 74.9 0)
+		(at 43.8 74.9 0)
 		(layer "B.SilkS")
 		(effects
@@
 		)
 	)
-	(gr_text "2-\n\n2+\n\n1-\n\n1+\n\nGND"
+	(gr_text "4-\n\n4+\n\n3-\n\n3+\n\nGND"
 		(at 74.65 74.9 0)
 		(layer "B.SilkS")
@@
 	)
 	(gr_text "4-\n\n4+\n\n3-\n\n3+\n\nGND"
-		(at 43.75 74.9 0)
+		(at 28.2 74.9 0)
 		(layer "B.SilkS")
 		(effects
@@
 	)
 	(gr_text "8-\n\n8+\n\n7-\n\n7+\n\nGND"
-		(at 43.85 56.9 0)
+		(at 28.2 56.9 0)
 		(layer "B.SilkS")
 		(effects
@@
 	)
 	(gr_text "6-\n\n6+\n\n5-\n\n5+\n\nGND"
-		(at 28.2 56.9 0)
+		(at 43.85 56.9 0)
 		(layer "B.SilkS")
 		(effects
@@
 		)
 	)
-	(gr_text "Michael Larson"
-		(at 68 87.8 0)
-		(layer "B.SilkS")
-		(effects
-			(font
-				(size 2 2)
-				(thickness 0.4)
-				(bold yes)
-			)
-			(justify left bottom mirror)
-		)
-	)
